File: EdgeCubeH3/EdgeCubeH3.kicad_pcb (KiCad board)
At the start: 2 copper layers, 52 x 52 mm, 19 parts, among them U1 H3, U2 K4B4G1646Q

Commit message: Schematic update, PCB started
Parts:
- added C11: 1u, Capacitor_SMD:C_0603_1608Metric, F.Cu at (184.1, 120.0)
- added C12: 10u, Capacitor_SMD:C_0603_1608Metric, F.Cu at (177.1, 122.0)
- added C13: 10u, Capacitor_SMD:C_0603_1608Metric, F.Cu at (174.1, 122.0)
- added C14: 22p, Capacitor_SMD:C_0603_1608Metric, F.Cu at (172.6, 115.7)
- added C15: 10u, Capacitor_SMD:C_0603_1608Metric, F.Cu at (177.0, 113.0)
- added C16: 10u, Capacitor_SMD:C_0603_1608Metric, F.Cu at (174.0, 113.0)
- added C17: 22p, Capacitor_SMD:C_0603_1608Metric, F.Cu at (172.5, 106.7)
- added C18: 10u, Capacitor_SMD:C_0603_1608Metric, F.Cu at (176.8, 104.0)
- added C19: 10u, Capacitor_SMD:C_0603_1608Metric, F.Cu at (173.8, 104.0)
- added C20: 15p, Capacitor_SMD:C_0603_1608Metric, F.Cu at (172.2, 97.6)
- added C21: 2u2, Capacitor_SMD:C_0603_1608Metric, F.Cu at (198.8, 120.0)
- added C22: 2u2, Capacitor_SMD:C_0603_1608Metric, F.Cu at (198.8, 122.5)
- added C23: 4u7, Capacitor_SMD:C_0603_1608Metric, F.Cu at (192.3, 84.5)
- added C24: 15p, Capacitor_SMD:C_0603_1608Metric, F.Cu at (160.3, 119.4)
- added C25: 15p, Capacitor_SMD:C_0603_1608Metric, F.Cu at (163.1, 117.0)
- added C26: 15p, Capacitor_SMD:C_0603_1608Metric, F.Cu at (164.8, 114.5)
- added C27: 15p, Capacitor_SMD:C_0603_1608Metric, F.Cu at (164.8, 109.5)
- added C28: 100n, Capacitor_SMD:C_0402_1005Metric, F.Cu at (199.7, 94.3)
- added C29: 4u7, Capacitor_SMD:C_0603_1608Metric, F.Cu at (192.3, 97.0)
- added C30: 100n, Capacitor_SMD:C_0603_1608Metric, F.Cu at (196.3, 84.5)
- added C31: 100n, Capacitor_SMD:C_0402_1005Metric, F.Cu at (199.7, 96.3)
- added C32: 100n, Capacitor_SMD:C_0402_1005Metric, F.Cu at (199.7, 98.3)
- added C33: 100n, Capacitor_SMD:C_0402_1005Metric, F.Cu at (199.7, 100.2)
- added C34: 100n, Capacitor_SMD:C_0402_1005Metric, F.Cu at (199.7, 102.2)
- added C35: 10u, Capacitor_SMD:C_0603_1608Metric, F.Cu at (196.3, 87.0)
- added C36: 10u, Capacitor_SMD:C_0603_1608Metric, F.Cu at (196.3, 89.5)
- added C37: 100n, Capacitor_SMD:C_0402_1005Metric, F.Cu at (202.6, 94.3)
- added C38: 10u, Capacitor_SMD:C_0603_1608Metric, F.Cu at (196.3, 92.0)
- added C39: 100n, Capacitor_SMD:C_0402_1005Metric, F.Cu at (202.6, 96.3)
- added C40: 100n, Capacitor_SMD:C_0402_1005Metric, F.Cu at (202.6, 98.3)
- added C41: 100n, Capacitor_SMD:C_0402_1005Metric, F.Cu at (202.6, 100.2)
- added C42: 100n, Capacitor_SMD:C_0402_1005Metric, F.Cu at (202.6, 102.2)
- added C43: 1u, Capacitor_SMD:C_0603_1608Metric, F.Cu at (139.0, 112.8)
- added C44: 1u, Capacitor_SMD:C_0603_1608Metric, B.Cu at (139.9, 89.0)
- added D1: SS12, Diode_SMD:D_SMA, F.Cu at (175.0, 90.6)
- added D2: 1N5819WS, Diode_SMD:D_SOD-323, B.Cu at (147.9, 125.8)
- added D4: LED, LED_SMD:LED_0805_2012Metric, F.Cu at (207.0, 129.0)
- added D5: LED, LED_SMD:LED_0805_2012Metric, F.Cu at (207.0, 132.0)
- added J1: USB PWR, Connector_USB:USB_C_Receptacle_HRO_TYPE-C-31-M-12, F.Cu at (137.9, 80.6)
- added J3: USB_A_Stacked, Connector_USB:USB_A_CUI_UJ2-ADH-TH_Horizontal_Stacked, F.Cu at (134.1, 95.5)
- added J4: GPDI_A, Connector_Video:HDMI_A_Molex_208658-1001_Horizontal, F.Cu at (152.9, 125.0)
- added J5: 93626-3006, rj45:936263006, F.Cu at (141.4, 114.5)
- added J6: DBG UART, Connector_PinHeader_2.54mm:PinHeader_1x03_P2.54mm_Vertical, B.Cu at (165.0, 122.8)
- added J7: GPIO, Connector_PinHeader_2.54mm:PinHeader_2x13_P2.54mm_Vertical, F.Cu at (177.2, 79.9)
- added J8: Micro_SD_Card_Det1, icepi:microSD_TF-01A, B.Cu at (172.2, 93.1)
- added L1: 2u2, Inductor_SMD:L_APV_APH0420, F.Cu at (170.2, 119.6)
- added L2: 2u2, Inductor_SMD:L_APV_APH0420, F.Cu at (170.1, 110.6)
- added L3: 2u2, Inductor_SMD:L_APV_APH0420, F.Cu at (169.8, 101.6)
- added Q1: NPN, Package_TO_SOT_SMD:TSOT-23, F.Cu at (176.0, 94.2)
- added Q2: PMOS, Package_TO_SOT_SMD:SOT-23W, F.Cu at (189.0, 126.0)
- added Q3: AO3404, Package_TO_SOT_SMD:SOT-23, B.Cu at (152.2, 125.9)
- added Q4: NPN, Package_TO_SOT_SMD:TSOT-23, F.Cu at (206.7, 104.9)
- added R10: 200K, Capacitor_SMD:C_0603_1608Metric, F.Cu at (175.7, 106.7)
- added R11: 100K, Capacitor_SMD:C_0603_1608Metric, F.Cu at (177.3, 106.7)
- added R12: 300K, Capacitor_SMD:C_0603_1608Metric, F.Cu at (174.1, 106.7)
- added R13: 10K, Resistor_SMD:R_0603_1608Metric, F.Cu at (173.8, 97.6)
- added R14: 12K, Resistor_SMD:R_0603_1608Metric, F.Cu at (175.4, 97.6)
- added R15: 33K, Resistor_SMD:R_0603_1608Metric, F.Cu at (177.0, 97.8)
- added R16: 33K, Resistor_SMD:R_0603_1608Metric, F.Cu at (173.0, 94.2)
- added R17: 10K, Resistor_SMD:R_0603_1608Metric, F.Cu at (169.2, 106.6)
- added R18: 10K, Resistor_SMD:R_0603_1608Metric, F.Cu at (171.5, 94.2)
- added R19: 100K, Resistor_SMD:R_0805_2012Metric_Pad1.20x1.40mm_HandSolder, F.Cu at (187.0, 131.0)
- added R20: 5K6, Resistor_SMD:R_0603_1608Metric, F.Cu at (198.8, 125.0)
- added R21: 2K, Resistor_SMD:R_0603_1608Metric, F.Cu at (198.8, 127.5)
- added R22: 2K, Resistor_SMD:R_0603_1608Metric, F.Cu at (198.8, 130.0)
- added R23: 30K, Resistor_SMD:R_0603_1608Metric, B.Cu at (155.9, 125.8)
- added R24: 5K6, Resistor_SMD:R_0603_1608Metric_Pad0.98x0.95mm_HandSolder, F.Cu at (188.1, 84.5)
- added R25: 470R, Resistor_SMD:R_0603_1608Metric_Pad0.98x0.95mm_HandSolder, F.Cu at (188.1, 87.0)
- added R26: 470R, Resistor_SMD:R_0603_1608Metric, B.Cu at (129.8, 122.0)
- added R27: 470R, Resistor_SMD:R_0603_1608Metric, B.Cu at (129.8, 118.4)
- added R28: 470R, Resistor_SMD:R_0603_1608Metric, F.Cu at (202.8, 125.0)
- added R29: 470R, Resistor_SMD:R_0603_1608Metric, F.Cu at (202.8, 127.5)
- added R30: 120R, Resistor_SMD:R_0603_1608Metric, F.Cu at (168.0, 127.9)
- added R31: 120R, Resistor_SMD:R_0603_1608Metric, F.Cu at (168.0, 125.4)
- added R32: 10K, Resistor_SMD:R_0603_1608Metric, F.Cu at (206.8, 120.0)
- added R33: 33R, Resistor_SMD:R_0603_1608Metric_Pad0.98x0.95mm_HandSolder, F.Cu at (188.1, 89.5)
- added R34: 47K, Resistor_SMD:R_0603_1608Metric, F.Cu at (206.8, 122.5)
- added R35: 47K, Resistor_SMD:R_0603_1608Metric, F.Cu at (206.8, 125.0)
- added R36: 56K, Resistor_SMD:R_0603_1608Metric_Pad0.98x0.95mm_HandSolder, F.Cu at (188.1, 92.0)
- added R37: 10K, Resistor_SMD:R_0603_1608Metric_Pad0.98x0.95mm_HandSolder, F.Cu at (188.1, 94.5)
- added R38: 10K, Resistor_SMD:R_0603_1608Metric_Pad0.98x0.95mm_HandSolder, F.Cu at (188.1, 97.0)
- added R39: 10K, Resistor_SMD:R_0603_1608Metric_Pad0.98x0.95mm_HandSolder, F.Cu at (188.1, 99.5)
- added R40: 51K, Resistor_SMD:R_0603_1608Metric_Pad0.98x0.95mm_HandSolder, F.Cu at (188.1, 102.1)
- added R41: 51K, Resistor_SMD:R_0603_1608Metric_Pad0.98x0.95mm_HandSolder, F.Cu at (188.1, 104.6)
- added R42: 10M, Resistor_SMD:R_0603_1608Metric, F.Cu at (167.8, 107.5)
- added R43: 3K, Resistor_SMD:R_0603_1608Metric, F.Cu at (158.2, 68.6)
- added R44: 3K, Resistor_SMD:R_0603_1608Metric, F.Cu at (158.2, 71.1)
- added R45: 3K, Resistor_SMD:R_0603_1608Metric, F.Cu at (158.2, 73.6)
- added R46: 3K, Resistor_SMD:R_0603_1608Metric, F.Cu at (158.2, 76.1)
- added R6: 10R, Resistor_SMD:R_1206_3216Metric, F.Cu at (173.9, 87.6)
- added R7: 680K, Capacitor_SMD:C_0603_1608Metric, F.Cu at (175.8, 115.7)
- added R8: 75K, Capacitor_SMD:C_0603_1608Metric, F.Cu at (177.4, 115.7)
- added R9: 680K, Capacitor_SMD:C_0603_1608Metric, F.Cu at (174.2, 115.7)
- added SW1: RST, Button_Switch_SMD:Button_6x3mm, F.Cu at (203.3, 85.8)
- added SW2: PWR, Button_Switch_SMD:Button_6x3mm, F.Cu at (203.3, 90.8)
- added TP1: UBOOT, TestPoint:TestPoint_Pad_D1.0mm, F.Cu at (205.5, 94.9)
- added TP2: PWR_KEY, TestPoint:TestPoint_Pad_D1.0mm, F.Cu at (205.5, 97.9)
- added TP3: TV, TestPoint:TestPoint_Pad_D1.0mm, F.Cu at (205.5, 101.0)
- added TP4: supercap, TestPoint:TestPoint_Pad_1.0x1.0mm, F.Cu at (174.9, 85.3)
- added TP5: gnd, TestPoint:TestPoint_Pad_1.0x1.0mm, F.Cu at (177.3, 85.2)
- added U10: USBLC6-4SC6, Package_TO_SOT_SMD:SOT-23-6, B.Cu at (141.4, 99.4)
- added U11: USBLC6-4SC6, Package_TO_SOT_SMD:SOT-23-6, F.Cu at (155.4, 117.4)
- added U12: USBLC6-4SC6, Package_TO_SOT_SMD:SOT-23-6, F.Cu at (151.6, 117.4)
- added U13: USBLC6-4SC6, Package_TO_SOT_SMD:SOT-23-6, F.Cu at (147.8, 117.4)
- added U3: USBLC6-2SC6, Package_TO_SOT_SMD:SOT-23-6, B.Cu at (137.7, 80.7)
- added U4: SY6280AAC, Package_TO_SOT_SMD:SOT-23-5, B.Cu at (130.0, 99.0)
- added U5: SY8089AAAC, SY8089:SY8089AAAC_SGY, F.Cu at (176.4, 119.3)
- added U6: SY8089AAAC, SY8089:SY8089AAAC_SGY, F.Cu at (176.3, 110.3)
- added U7: SY8032, Package_TO_SOT_SMD:SOT-23-6, F.Cu at (176.0, 101.4)
- added U8: W25Q128JVP, Package_SON:WSON-8-1EP_6x5mm_P1.27mm_EP3.4x4.3mm, B.Cu at (144.2, 90.4)
- added Y1: 24M, Crystal:Crystal_SMD_3225-4Pin_3.2x2.5mm, F.Cu at (160.2, 116.9)
- added Y2: 32K, Crystal:Crystal_SMD_3225-4Pin_3.2x2.5mm, F.Cu at (164.8, 112.0)
- U1: footprint Lib:BGA347_H3_AWT-M -> cm0:FBGA-347_14x14mm_Layout21x21_P0.65mm
- moved C2 34.0 mm to (185.6, 113.8)
- moved C9 34.0 mm to (193.1, 113.8)
- moved C1 34.0 mm to (183.1, 113.8)
- moved C10 34.0 mm to (195.6, 113.8)
- moved C3 34.0 mm to (182.8, 110.4)
- moved C4 34.0 mm to (184.8, 110.4)
- moved C5 34.0 mm to (186.7, 110.4)
- moved C6 34.0 mm to (188.7, 110.4)
- moved C7 34.0 mm to (188.1, 113.8)
- moved C8 34.0 mm to (190.6, 113.8)
- moved R3 34.0 mm to (198.1, 113.8)
- moved R4 34.0 mm to (200.6, 113.8)
- moved R5 34.0 mm to (203.2, 113.8)
- moved U1 14.4 mm to (154.2, 106.5), turned to 90 degrees
- moved U2 7.26 mm to (157.0, 91.0), turned to 90 degrees
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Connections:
- net VDD_DRAM renamed +1V35
- U1 pad A19: unconnected-(U1F-PF1-PadA19) -> /SoC/SDC0_D0
- U1 pad A2: unconnected-(U1D-EPHY_LINK_LED-PadA2) -> /SoC/EPHY_LINK_LED
- U1 pad A21: Net-(U1B-GND-PadA21) -> GND
- U1 pad A3: unconnected-(U1D-EPHY_TXN-PadA3) -> /SoC/EPHY_TX-
- U1 pad A4: unconnected-(U1D-EPHY_RXN-PadA4) -> /SoC/EPHY_RX-
- U1 pad A5: unconnected-(U1E-USB_D0+-PadA5) -> USB_D0+
- U1 pad A7: unconnected-(U1E-USB_D2+-PadA7) -> USB_D2+
- U1 pad A8: unconnected-(U1E-USB_D2--PadA8) -> USB_D2-
- U1 pad AA1: Net-(U1B-GND-PadA21) -> GND
- U1 pad AA6: unconnected-(U1G-NMI-PadAA6) -> Net-(U1G-NMI)
- U1 pad B13: unconnected-(U1F-PA18-PadB13) -> TWI1_SCK
- U1 pad B14: unconnected-(U1F-PA19-PadB14) -> TWI1_SDA
- U1 pad B15: unconnected-(U1C-PC3-PadB15) -> SPI0_CS
- U1 pad B16: unconnected-(U1C-PC2-PadB16) -> SPI0_CLK
- U1 pad B3: unconnected-(U1D-EPHY_TXP-PadB3) -> /SoC/EPHY_TX+
- U1 pad B4: unconnected-(U1D-EPHY_RXP-PadB4) -> /SoC/EPHY_RX+
- U1 pad B5: unconnected-(U1E-USB_D0--PadB5) -> USB_D0-
- U1 pad B6: unconnected-(U1E-USB_D1+-PadB6) -> USB_D1+
- U1 pad B7: unconnected-(U1E-USB_D1--PadB7) -> USB_D1-
- U1 pad C13: unconnected-(U1F-PA12-PadC13) -> TWI0_SDA
- U1 pad C14: unconnected-(U1F-PA17-PadC14) -> STATUS_LED
- U1 pad C15: unconnected-(U1C-PC0-PadC15) -> SPI0_MOSI
- U1 pad C16: unconnected-(U1C-PC1-PadC16) -> SPI0_MISO
- U1 pad C20: unconnected-(U1F-PF5-PadC20) -> /SoC/SDC0_D2
- U1 pad D11: unconnected-(U1F-PA0-PadD11) -> UART2_TX
- U1 pad D15: unconnected-(U1F-PA16-PadD15) -> SPI1_MISO
- U1 pad D19: unconnected-(U1F-PF0-PadD19) -> /SoC/SDC0_D1
- U1 pad D20: unconnected-(U1F-PF2-PadD20) -> Net-(U1F-PF2)
- U1 pad D3: unconnected-(U1C-PG7-PadD3) -> UART1_RX
- U1 pad D5: unconnected-(U1F-PA1-PadD5) -> UART2_RX
- U1 pad D6: unconnected-(U1F-PA2-PadD6) -> UART2_RTS
- U1 pad D8: unconnected-(U1F-PA7-PadD8) -> PA7
- U1 pad E11: unconnected-(U1F-PA10-PadE11) -> PA10
- U1 pad E13: unconnected-(U1F-PA3-PadE13) -> UART2_CTS
- U1 pad E14: unconnected-(U1F-PA6-PadE14) -> PA6
- U1 pad E15: unconnected-(U1F-PA13-PadE15) -> SPI1_CS
- U1 pad E2: unconnected-(U1D-GPDI_CLK--PadE2) -> /SoC/GPDI_CLK-
- U1 pad E21: unconnected-(U1F-PF4-PadE21) -> /SoC/SDC0_D3
- U1 pad F1: unconnected-(U1D-GPDI_D0--PadF1) -> /SoC/GPDI_D0-
- U1 pad F10: unconnected-(U1D-TVOUT-PadF10) -> Net-(U1D-TVOUT)
- U1 pad F11: unconnected-(U1F-PA11-PadF11) -> TWI0_SCK
- U1 pad F14: unconnected-(U1F-PA15-PadF14) -> SPI1_MOSI
- U1 pad F18: unconnected-(U1F-PF3-PadF18) -> /SoC/SDC0_CMD
- U1 pad F2: unconnected-(U1D-GPDI_CLK+-PadF2) -> /SoC/GPDI_CLK+
- U1 pad F5: unconnected-(U1F-PA4-PadF5) -> UART0_TX
- U1 pad F6: unconnected-(U1D-EPHY_RTX-PadF6) -> Net-(U1D-EPHY_RTX)
- U1 pad F7: unconnected-(U1D-EPHY_SPD_LED-PadF7) -> /SoC/EPHY_SPD_LED
- U1 pad F8: unconnected-(U1D-EPHY_VDD-PadF8) -> +1V2
- U1 pad G1: unconnected-(U1D-GPDI_D0+-PadG1) -> /SoC/GPDI_D0+
- U1 pad G10: unconnected-(U1B-VDD-EFUSE-PadG10) -> Net-(U1B-VDD-EFUSE)
- U1 pad G11: unconnected-(U1E-VCC_USB-PadG11) -> VCC_IO
- U1 pad G12: unconnected-(U1F-PA14-PadG12) -> SPI1_CLK
- U1 pad G13: unconnected-(U1B-VCC-IO-PadG13) -> VCC_IO
- U1 pad G14: unconnected-(U1B-VCC-IO-PadG14) -> VCC_IO
- U1 pad G15: unconnected-(U1B-VCC-IO-PadG15) -> VCC_IO
- U1 pad G18: unconnected-(U1F-PF6-PadG18) -> /SoC/SDC0_DET
- U1 pad G2: unconnected-(U1D-GPDI_D1--PadG2) -> /SoC/GPDI_D1-
- U1 pad G4: unconnected-(U1C-PG6-PadG4) -> UART1_TX
- U1 pad G5: unconnected-(U1D-GPDI_CEC-PadG5) -> /SoC/GPDI_CEC
- U1 pad G7: unconnected-(U1D-EPHY_VCC-PadG7) -> +3V3
- U1 pad G8: Net-(U1B-GND-PadA21) -> GND
- U1 pad G9: unconnected-(U1D-V33_TV-PadG9) -> +3V3
- U1 pad H10: unconnected-(U1B-VDD-SYS-PadH10) -> +1V2
- U1 pad H11: unconnected-(U1B-VDD-EFUSEEBP-PadH11) -> +3V3
- U1 pad H12: Net-(U1B-GND-PadA21) -> GND
- U1 pad H13: unconnected-(U1B-VCC-IO-PadH13) -> VCC_IO
- U1 pad H14: unconnected-(U1B-VCC-IO-PadH14) -> VCC_IO
- U1 pad H15: Net-(U1B-GND-PadA21) -> GND
- U1 pad H2: unconnected-(U1D-GPDI_D1+-PadH2) -> /SoC/GPDI_D1+
- U1 pad H3: unconnected-(U1D-GPDI_SCL-PadH3) -> /SoC/GPDI_SCL
- U1 pad H6: unconnected-(U1F-PA5-PadH6) -> UART0_RX
- U1 pad H7: unconnected-(U1C-VCC-PG-PadH7) -> VCC_IO
- U1 pad H8: unconnected-(U1D-GND_TV-PadH8) -> GND
- U1 pad J1: unconnected-(U1D-GPDI_D2+-PadJ1) -> /SoC/GPDI_D2+
- U1 pad J10: unconnected-(U1B-VDD-SYS-PadJ10) -> +1V2
- U1 pad J11: unconnected-(U1B-VDD-SYS-PadJ11) -> +1V2
- U1 pad J12: unconnected-(U1B-VDD-SYS-PadJ12) -> +1V2
- U1 pad J13: Net-(U1B-GND-PadA21) -> GND
- U1 pad J14: unconnected-(U1B-VCC-IO-PadJ14) -> VCC_IO
- U1 pad J15: unconnected-(U1F-VCC_PD-PadJ15) -> VCC_IO
- U1 pad J16: Net-(U1B-GND-PadA21) -> GND
- U1 pad J2: unconnected-(U1D-GPDI_D2--PadJ2) -> /SoC/GPDI_D2-
- U1 pad J6: unconnected-(U1D-GPDI_VCC-PadJ6) -> +3V3
- U1 pad J7: unconnected-(U1B-VDD-CPUS-PadJ7) -> +1V2
- U1 pad J8: unconnected-(U1B-VDD-CPUS-PadJ8) -> +1V2
- U1 pad J9: Net-(U1B-GND-PadA21) -> GND
- U1 pad K1: unconnected-(U1G-X24MOUT-PadK1) -> Net-(U1G-X24MOUT)
- U1 pad K10: unconnected-(U1B-VDD-SYS-PadK10) -> +1V2
- U1 pad K11: unconnected-(U1B-VDD-SYS-PadK11) -> +1V2
- U1 pad K12: unconnected-(U1B-VDD-SYS-PadK12) -> +1V2
- U1 pad K13: Net-(U1B-GND-PadA21) -> GND
- U1 pad K14: Net-(U1B-GND-PadA21) -> GND
- U1 pad K15: Net-(U1B-GND-PadA21) -> GND
- U1 pad K16: Net-(U1B-GND-PadA21) -> GND
- U1 pad K2: unconnected-(U1G-X24MIN-PadK2) -> Net-(U1G-X24MIN)
- U1 pad K3: unconnected-(U1D-GPDI_SDA-PadK3) -> /SoC/GPDI_SDA
- U1 pad K6: unconnected-(U1G-VCC_RTC-PadK6) -> +3V3
- U1 pad K7: Net-(U1B-GND-PadA21) -> GND
- U1 pad K8: Net-(U1B-GND-PadA21) -> GND
- U1 pad K9: Net-(U1B-GND-PadA21) -> GND
- U1 pad L10: unconnected-(U1B-VDD-SYS-PadL10) -> +1V2
- U1 pad L11: unconnected-(U1B-VDD-SYS-PadL11) -> +1V2
- U1 pad L12: unconnected-(U1B-VDD-SYS-PadL12) -> +1V2
- U1 pad L13: unconnected-(U1B-VDD-SYS-PadL13) -> +1V2
- U1 pad L14: unconnected-(U1B-VDD-SYS-PadL14) -> +1V2
- U1 pad L15: Net-(U1B-GND-PadA21) -> GND
- U1 pad L8: Net-(U1B-GND-PadA21) -> GND
- U1 pad L9: Net-(U1B-GND-PadA21) -> GND
- U1 pad M10: Net-(U1B-GND-PadA21) -> GND
- U1 pad M11: Net-(U1B-GND-PadA21) -> GND
- U1 pad M12: Net-(U1B-GND-PadA21) -> GND
- U1 pad M13: Net-(U1B-GND-PadA21) -> GND
- U1 pad M14: Net-(U1B-GND-PadA21) -> GND
- U1 pad M15: Net-(U1B-GND-PadA21) -> GND
- U1 pad M2: unconnected-(U1D-GPDI_HPD-PadM2) -> /SoC/GPDI_HPD
- U1 pad M4: unconnected-(U1G-RTC_VIO-PadM4) -> +1V2
- U1 pad M5: unconnected-(U1D-GPDI_GND-PadM5) -> GND
- U1 pad M6: unconnected-(U1F-PL9-PadM6) -> PWR_DRAM_EN
- U1 pad M7: Net-(U1B-GND-PadA21) -> GND
- U1 pad M8: Net-(U1B-GND-PadA21) -> GND
- U1 pad M9: Net-(U1B-GND-PadA21) -> GND
- U1 pad N10: Net-(U1B-GND-PadA21) -> GND
- U1 pad N11: Net-(U1B-GND-PadA21) -> GND
- U1 pad N12: Net-(U1B-GND-PadA21) -> GND
- U1 pad N13: Net-(U1B-GND-PadA21) -> GND
- U1 pad N14: Net-(U1B-GND-PadA21) -> GND
- U1 pad N15: Net-(U1B-GND-PadA21) -> GND
- U1 pad N2: unconnected-(U1F-PL4-PadN2) -> Net-(U1F-PL4)
- U1 pad N3: unconnected-(U1G-VCC_PLL-PadN3) -> +3V3
- U1 pad N7: Net-(U1B-GND-PadA21) -> GND
- U1 pad N8: unconnected-(U1B-VDD-CPUX-PadN8) -> +1V2
- U1 pad N9: Net-(U1B-GND-PadA21) -> GND
- U1 pad P10: Net-(U1B-GND-PadA21) -> GND
- U1 pad P11: Net-(U1B-GND-PadA21) -> GND
- U1 pad P12: Net-(U1B-GND-PadA21) -> GND
- U1 pad P13: Net-(U1B-GND-PadA21) -> GND
- U1 pad P14: Net-(U1B-GND-PadA21) -> GND
- U1 pad P15: Net-(U1B-GND-PadA21) -> GND
- U1 pad P6: unconnected-(U1B-VDD-CPUX-PadP6) -> +1V2
- U1 pad P7: unconnected-(U1B-VDD-CPUX-PadP7) -> +1V2
- U1 pad P8: unconnected-(U1B-VDD-CPUX-PadP8) -> +1V2
- U1 pad P9: unconnected-(U1B-VDD-CPUX-PadP9) -> +1V2
- U1 pad R1: unconnected-(U1F-PL3-PadR1) -> Net-(U1F-PL3)
- U1 pad R10: Net-(U1B-GND-PadA21) -> GND
- U1 pad R11: Net-(U1B-GND-PadA21) -> GND
- U1 pad R12: Net-(U1B-GND-PadA21) -> GND
- U1 pad R13: Net-(U1B-GND-PadA21) -> GND
- U1 pad R14: Net-(U1B-GND-PadA21) -> GND
- U1 pad R2: unconnected-(U1F-PL5-PadR2) -> VCC_IO_EN
- U1 pad R6: unconnected-(U1B-VDD-CPUX-PadR6) -> +1V2
- U1 pad R7: unconnected-(U1B-VDD-CPUX-PadR7) -> +1V2
- U1 pad R8: unconnected-(U1B-VDD-CPUX-PadR8) -> +1V2
- U1 pad R9: Net-(U1B-GND-PadA21) -> GND
- U1 pad T10: unconnected-(U1G-VDD-CPUFB-PadT10) -> PWR_CPUFB
- U1 pad T11: Net-(U1B-GND-PadA21) -> GND
- U1 pad T2: unconnected-(U1F-PL8-PadT2) -> PWR_STB_EN
- U1 pad T4: unconnected-(U1F-PL6-PadT4) -> CPUX_VSET
- U1 pad T6: unconnected-(U1B-VDD-CPUX-PadT6) -> +1V2
- U1 pad T7: unconnected-(U1B-VDD-CPUX-PadT7) -> +1V2
- U1 pad T8: unconnected-(U1B-VDD-CPUX-PadT8) -> +1V2
- U1 pad T9: unconnected-(U1G-GND-CPUFB-PadT9) -> GND
- U1 pad U3: unconnected-(U1H-AGND-PadU3) -> GND
- U1 pad U4: unconnected-(U1G-X32KOUT-PadU4) -> Net-(U1G-X32KOUT)
- U1 pad U6: unconnected-(U1B-VDD-CPUX-PadU6) -> +1V2
- U1 pad U9: unconnected-(U1B-VDD-CPUX-PadU9) -> +1V2
- U1 pad V2: unconnected-(U1F-PL10-PadV2) -> PWR_LED
- U1 pad V3: unconnected-(U1H-AVCC-PadV3) -> +3V3
- U1 pad V5: unconnected-(U1G-X32KIN-PadV5) -> Net-(U1G-X32KIN)
- U1 pad V6: unconnected-(U1G-RESET-PadV6) -> /SoC/RESET
- U1 pad W6: unconnected-(U1G-UBOOT-PadW6) -> Net-(U1G-UBOOT)
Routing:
- net GND: track 0.00 -> 64.4 mm, vias 0 -> 53
- net /SoC/GPDI_CEC: track 0.00 -> 24.5 mm, vias 0 -> 1
- net /SoC/GPDI_SDA: track 0.00 -> 22.7 mm, vias 0 -> 2
- net PWR_DRAM_EN: track 0.00 -> 22.1 mm
- net VBUS: track 0.00 -> 21.8 mm, vias 0 -> 1
- net +3V3: track 0.00 -> 21.5 mm
- net +1V35: track 0.00 -> 20.1 mm
- net +1V2: track 0.00 -> 19.8 mm, vias 0 -> 6
- net /SoC/GPDI_HPD: track 0.00 -> 17.7 mm, vias 0 -> 2
- net /SoC/GPDI_SCL: track 0.00 -> 16.0 mm
- net /ports/CEC: track 0.00 -> 15.8 mm, vias 0 -> 1
- net /SoC/GPDI_D2-: track 0.00 -> 12.2 mm
- net /SoC/GPDI_D1+: track 0.00 -> 11.9 mm
- net /SoC/GPDI_CLK+: track 0.00 -> 11.9 mm
- net /SoC/GPDI_D0-: track 0.00 -> 11.5 mm
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- added copper zone on F.Cu, net GND
- added copper zone on In1.Cu, net GND
- added copper zone on In4.Cu, net GND
- added copper zone on F.Cu, net Net-(U5-LX)
- added copper zone on F.Cu, net Net-(U6-LX)
- added copper zone on F.Cu, net Net-(U7-LX)
- added copper zone on F.Cu, net VBUS
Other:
- copper layers 2 -> 6

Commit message: PCB design at ~90%
- re-arrangement of components
- connecting dram
- connecting ports
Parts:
- C29, C30, C43, Q4, R20, R21, R22, R33, R37, R38, R39, R40, R41, R42: moved to B.Cu
- D4: value LED -> PWR
- D5: value LED -> STA
- R19: footprint Resistor_SMD:R_0805_2012Metric_Pad1.20x1.40mm_HandSolder -> Resistor_SMD:R_0603_1608Metric_Pad0.98x0.95mm_HandSolder
- R36: footprint Resistor_SMD:R_0603_1608Metric_Pad0.98x0.95mm_HandSolder -> Resistor_SMD:R_0603_1608Metric
- R5: footprint Resistor_SMD:R_0603_1608Metric -> Resistor_SMD:R_0402_1005Metric; moved to B.Cu
- U10: moved to F.Cu
- moved D4 89.8 mm to (128.7, 85.0)
- moved D5 89.7 mm to (128.7, 88.3)
- moved R28 81.4 mm to (131.9, 85.1), turned to 180 degrees
- moved R29 81.1 mm to (131.9, 88.2), turned to 180 degrees
- moved R20 72.1 mm to (130.6, 101.7)
- moved C21 63.5 mm to (139.9, 96.3), turned to -90 degrees
- moved C11 59.3 mm to (135.0, 86.7), turned to 180 degrees
- moved C23 52.9 mm to (144.3, 106.9), turned to 180 degrees
- moved R25 51.9 mm to (140.8, 108.5)
- moved R24 50.1 mm to (144.1, 108.5)
- moved R5 50.1 mm to (160.1, 88.2), turned to 0 degrees
- moved R21 49.3 mm to (149.5, 127.1), turned to -90 degrees
- moved R22 47.9 mm to (151.0, 127.1), turned to 90 degrees
- moved C30 44.9 mm to (172.9, 122.8)
- moved Q4 42.8 mm to (169.0, 125.1), turned to 180 degrees
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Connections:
- net Net-(J1-D+-PadA6) renamed /power/USB+
- net Net-(J1-D--PadA7) renamed /power/USB-
- U2 pad A3: /SoC/SDQ15 -> /SoC/SDQ12
- U2 pad A7: /SoC/SDQ12 -> /SoC/SDQ8
- U2 pad B8: /SoC/SDQ14 -> /SoC/SDQ9
- U2 pad C2: /SoC/SDQ11 -> /SoC/SDQ15
- U2 pad C3: /SoC/SDQ9 -> /SoC/SDQ14
- U2 pad D7: /SoC/SDQ8 -> /SoC/SDQ11
- U2 pad E3: /SoC/SDQ0 -> /SoC/SDQ5
- U2 pad F2: /SoC/SDQ2 -> /SoC/SDQ6
- U2 pad F7: /SoC/SDQ1 -> /SoC/SDQ2
- U2 pad F8: /SoC/SDQ3 -> /SoC/SDQ0
- U2 pad G2: /SoC/SDQ6 -> /SoC/SDQ3
- U2 pad H3: /SoC/SDQ4 -> /SoC/SDQ7
- U2 pad H7: /SoC/SDQ7 -> /SoC/SDQ4
- U2 pad H8: /SoC/SDQ5 -> /SoC/SDQ1
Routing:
- net USB_D0-: track 0.00 -> 45.9 mm, vias 0 -> 1
- net USB_D0+: track 0.00 -> 43.8 mm, vias 0 -> 1
- net GND: track 64.4 -> 106.2 mm, vias 53 -> 98
- net VREF: track 0.00 -> 36.3 mm, vias 0 -> 4
- net USB_D1-: track 0.00 -> 29.7 mm, vias 0 -> 2
- net USB_D1+: track 0.00 -> 29.2 mm, vias 0 -> 2
- net /SoC/SWE: track 0.00 -> 27.3 mm
- net /SoC/SBA0: track 0.00 -> 26.9 mm
- net /SoC/SBA2: track 0.00 -> 26.9 mm
- net /SoC/SCK+: track 0.00 -> 26.9 mm, vias 0 -> 2
- net /SoC/SCK-: track 0.00 -> 26.9 mm, vias 0 -> 2
- net /SoC/SA5: track 0.00 -> 26.9 mm
- net /SoC/SA3: track 0.00 -> 26.8 mm
- net PWR_CPUFB: track 1.62 -> 28.3 mm
- net /SoC/SA15: track 0.00 -> 26.0 mm, vias 0 -> 2
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
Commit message: PCB at 95%
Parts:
- removed SW1: RST, Button_Switch_SMD:Button_6x3mm
- removed SW2: PWR, Button_Switch_SMD:Button_6x3mm
- C22, C28, C3, C31, C32, C33, C34, C35, C36, C37, C38, C39, C4, C40, C41, C42, C5, C6, C7, C9, R34, R35, TP1, TP2, TP3: moved to B.Cu
- moved TP3 65.2 mm to (140.6, 107.2), turned to 180 degrees
- moved TP2 55.2 mm to (153.1, 115.0), turned to 180 degrees
- moved C37 53.0 mm to (151.2, 107.2)
- moved C10 52.8 mm to (151.1, 85.4), turned to -90 degrees
- moved C39 52.3 mm to (151.8, 108.5)
- moved C40 51.6 mm to (152.2, 109.5)
- moved C8 50.1 mm to (149.4, 85.4), turned to -90 degrees
- moved C41 49.4 mm to (154.2, 110.3)
- moved TP1 48.3 mm to (159.3, 108.9), turned to 180 degrees
- moved C9 47.9 mm to (154.8, 85.1), turned to 180 degrees
- moved C31 47.7 mm to (153.6, 108.6)
- moved C28 47.1 mm to (155.7, 111.0), turned to 90 degrees
- moved C42 46.0 mm to (156.7, 104.7), turned to 180 degrees
- moved C33 45.8 mm to (154.4, 107.1)
- moved R34 45.7 mm to (163.8, 107.2), turned to 180 degrees
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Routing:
- net VBUS: track 40.2 -> 201.2 mm, vias 6 -> 13
- net +3V3: track 29.8 -> 139.2 mm, vias 8 -> 13
- net PWR_LED: track 0.00 -> 94.4 mm, vias 0 -> 3
- net VCC_IO: track 12.8 -> 88.0 mm, vias 6 -> 8
- net /SoC/SDC0_DET: track 0.00 -> 56.0 mm, vias 0 -> 2
- net /SoC/SDC0_CMD: track 0.00 -> 42.7 mm, vias 0 -> 2
- net /SoC/SDC0_D0: track 0.00 -> 41.8 mm, vias 0 -> 2
- net TWI1_SCK: track 0.00 -> 41.6 mm, vias 0 -> 1
- net /SoC/SDC0_CLK: track 0.00 -> 37.0 mm, vias 0 -> 2
- net /SoC/SDC0_D1: track 0.00 -> 35.2 mm, vias 0 -> 2
- net /SoC/SDC0_D3: track 0.00 -> 32.8 mm, vias 0 -> 2
- net UART2_RTS: track 0.00 -> 30.8 mm, vias 0 -> 1
- net /SoC/EPHY_SPD_LED: track 0.00 -> 30.6 mm, vias 0 -> 1
- net SPI1_CLK: track 0.00 -> 29.8 mm
- net SPI1_MOSI: track 0.00 -> 29.1 mm, vias 0 -> 1
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- added copper zone on In2.Cu, net +1V2
- added copper zone on In2.Cu, net +1V35

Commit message: PCB at 98%
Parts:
- removed R43, R44, R45, R46: 3K, Resistor_SMD:R_0603_1608Metric
- moved R32 8.88 mm to (162.5, 123.4), turned to -90 degrees
- moved D5 0.22 mm to (128.9, 88.3)
- moved D4 0.20 mm to (128.9, 85.0)
- moved TP5 0.10 mm to (177.3, 85.3)
- moved R38 0.10 mm to (172.9, 129.1)
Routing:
- net VCC_IO: track 88.0 -> 158.4 mm, vias 8 -> 9
- net UART0_TX: track 0.00 -> 46.2 mm, vias 0 -> 2
- net UART0_RX: track 0.00 -> 45.9 mm
- net GND: track 122.7 -> 155.9 mm, vias 110 -> 114
- net /SoC/RESET: track 0.00 -> 25.4 mm, vias 0 -> 3
- net CPUX_VSET: track 1.74 -> 26.0 mm, vias 0 -> 2
- net VCC_IO_EN: track 1.69 -> 25.2 mm
- net PWR_DRAM_EN: track 22.1 -> 42.8 mm
- net PWR_STB_EN: track 8.21 -> 28.4 mm, vias 0 -> 2
- net +3V3: track 139.2 -> 144.4 mm
- net Net-(J6-Pin_3): track 2.18 -> 6.86 mm, vias 0 -> 1
- net +1V35: track 42.1 -> 46.7 mm
- net Net-(Q4-B): track 0.00 -> 4.28 mm
- net Net-(C29-Pad2): track 0.00 -> 3.22 mm

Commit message: Compleating PCB design
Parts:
- added C45: 100n, Resistor_SMD:R_0402_1005Metric, B.Cu at (155.8, 103.5)
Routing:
- net /SoC/SDC0_D2: track 28.5 -> 42.9 mm
- net /SoC/SDC0_D3: track 33.0 -> 41.9 mm
- net /SoC/SDC0_D1: track 35.6 -> 41.9 mm
- net /SoC/SDC0_CLK: track 37.0 -> 42.1 mm
- net GND: track 155.9 -> 156.8 mm
- net VREF: track 36.3 -> 37.0 mm
- added copper zone on In2.Cu, net GND
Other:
- board text added: "EdgeCubeH3"
- board text added: "EdgeCubeH3 rev.A"
- board text added: "Flash"
- board text added: "github.com/sentoxo/EdgeCubeH3 J.K. 20.05.2026 rev.A"

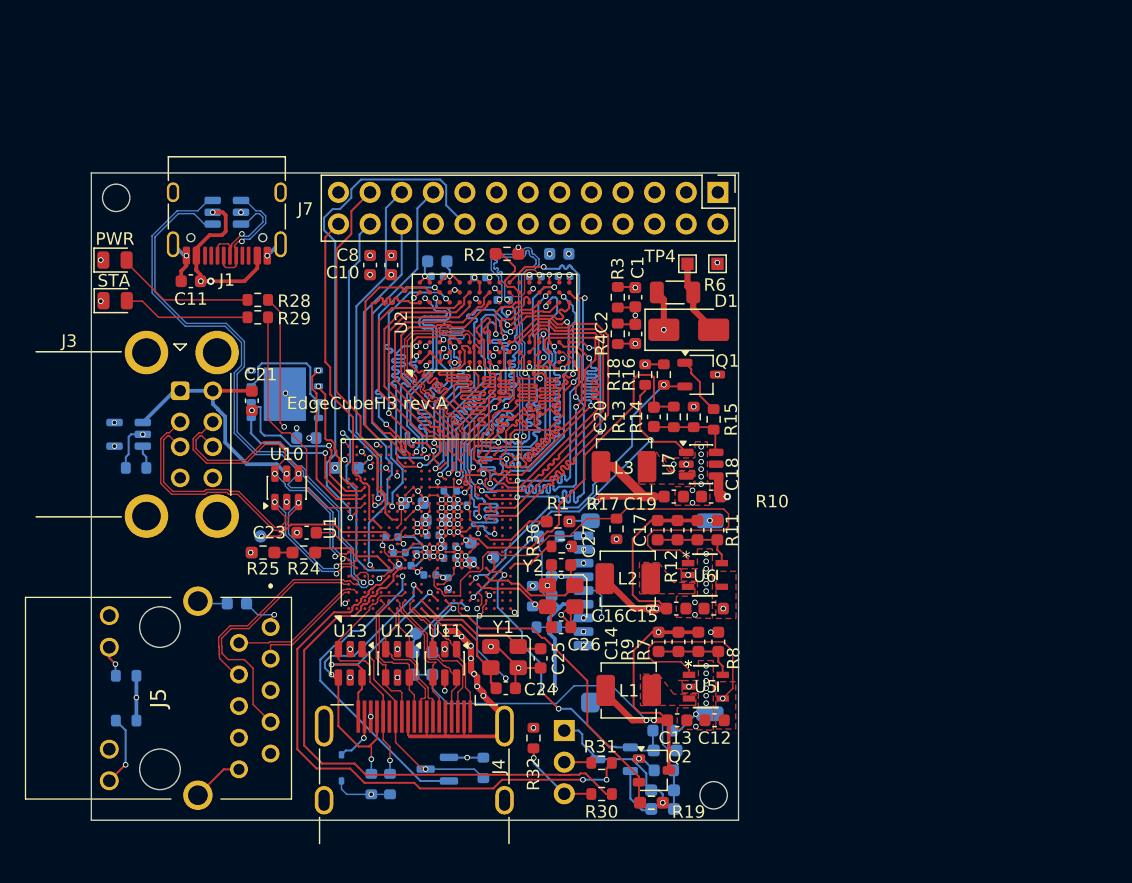
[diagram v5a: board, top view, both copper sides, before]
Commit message: Small changes to PCB, updated schematic and readme
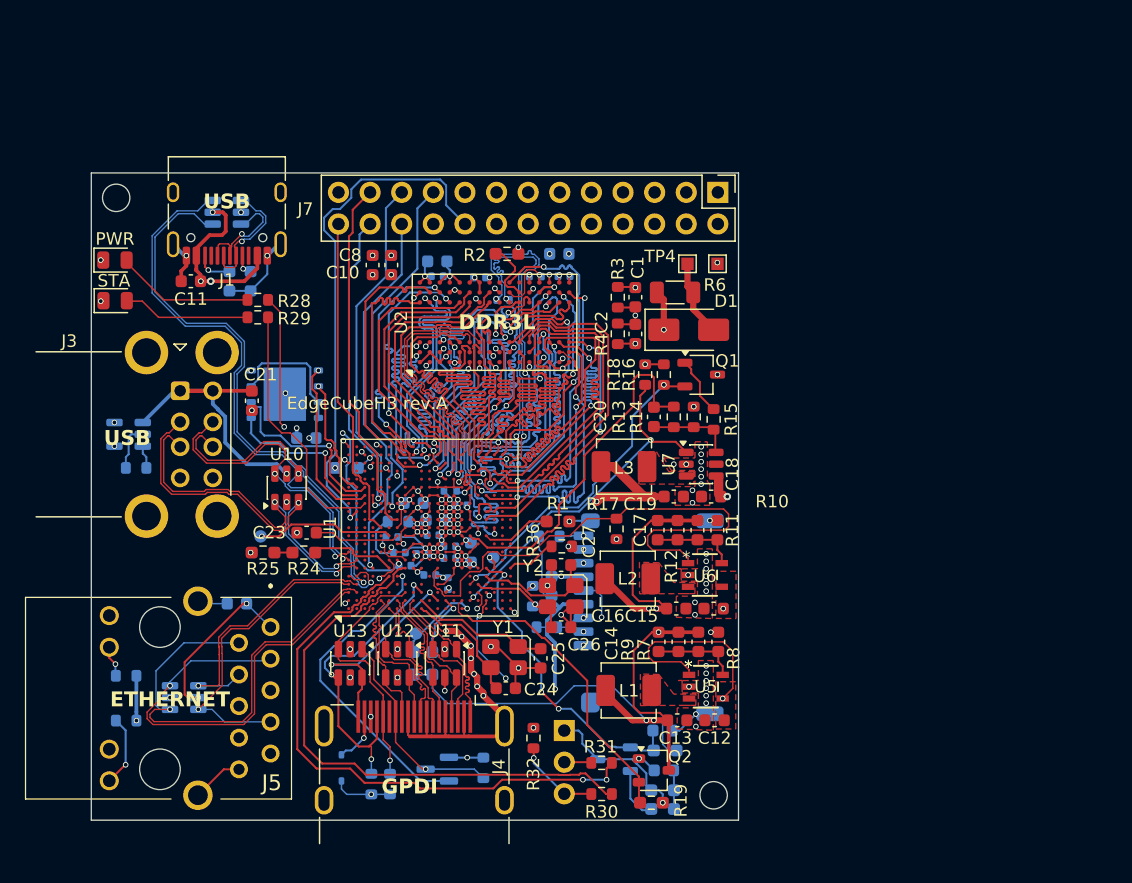
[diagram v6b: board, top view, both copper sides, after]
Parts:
- added R47: 2R2, Resistor_SMD:R_0603_1608Metric, B.Cu at (151.6, 106.0)
- added R48: 5K1, Capacitor_SMD:C_0603_1608Metric, B.Cu at (139.8, 86.7)
- added R49: 5K1, Capacitor_SMD:C_0603_1608Metric, B.Cu at (138.1, 86.7)
- added U14: USBLC6-4SC6, Package_TO_SOT_SMD:SOT-23-6, B.Cu at (134.5, 120.2)
- moved C8 0.20 mm to (149.6, 85.4)
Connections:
- C39 pad 1: +1V2 -> Net-(U1D-EPHY_VDD)
- J1 pad A5: unconnected-(J1-CC1-PadA5) -> Net-(J1-CC1)
- J1 pad B5: unconnected-(J1-CC2-PadB5) -> Net-(J1-CC2)
- U1 pad F8: +1V2 -> Net-(U1D-EPHY_VDD)
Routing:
- net +1V35: track 46.7 -> 88.8 mm
- net +1V2: track 39.5 -> 69.4 mm, vias 15 -> 14
- net /SoC/EPHY_TX-: track 9.13 -> 36.1 mm, vias 0 -> 1
- net /SoC/EPHY_TX+: track 11.4 -> 37.7 mm, vias 0 -> 1
- net VCC_IO: track 158.4 -> 169.3 mm, vias 9 -> 10
- net GND: track 156.8 -> 163.1 mm, vias 114 -> 115
- net /SoC/EPHY_RX+: track 17.1 -> 22.7 mm, vias 0 -> 1
- net Net-(J3-VBUS1): track 20.6 -> 25.8 mm
- net Net-(U1D-EPHY_VDD): track 0.00 -> 4.81 mm, vias 0 -> 1
- net /SoC/EPHY_RX-: track 21.2 -> 24.9 mm, vias 0 -> 1
- net Net-(J1-CC2): track 0.00 -> 3.01 mm, vias 0 -> 1
- net /SoC/GPDI_D0+: track 10.0 -> 12.0 mm
- net Net-(J1-CC1): track 0.00 -> 1.77 mm, vias 0 -> 1
- net /SoC/GPDI_D2+: track 10.8 -> 12.0 mm
- net SPI1_CLK: track 29.8 -> 29.0 mm
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- removed copper zone on In2.Cu, net +1V2
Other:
- board text added: "DDR3L"
- board text added: "ETHERNET"
- board text added: "G TX RX"
- board text added: "GPDI"
- board text added: "USB"
- board text added: "github.com/sentoxo/EdgeCubeH3 J.K. 21.05.2026 rev.A"
- board text added: "microSD"
- board text removed: "github.com/sentoxo/EdgeCubeH3 J.K. 20.05.2026 rev.A"

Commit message: Finalization of rev.A
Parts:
- removed TP4: supercap, TestPoint:TestPoint_Pad_1.0x1.0mm
- removed TP5: gnd, TestPoint:TestPoint_Pad_1.0x1.0mm
- added J2: SUPERCAP, Connector_PinHeader_1.27mm:PinHeader_1x02_P1.27mm_Vertical, F.Cu at (177.4, 85.5)
- J6: moved to F.Cu
- R48, R49: footprint Capacitor_SMD:C_0603_1608Metric -> Resistor_SMD:R_0603_1608Metric
- moved R32 14.6 mm to (177.1, 124.6), turned to 0 degrees
- turned J6 to 0 degrees
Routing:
- net Net-(J6-Pin_3): track 6.86 -> 15.7 mm, vias 1 -> 0
- net VCC_IO: track 169.3 -> 176.1 mm, vias 10 -> 9
- net SPI0_CLK: track 9.93 -> 16.0 mm
- net /SoC/SA0: track 24.9 -> 23.0 mm
- net GND: track 163.1 -> 164.9 mm, vias 115 -> 114
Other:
- board text added: "G"
- board text added: "RX"
- board text added: "TX"
- board text added: "USB-C"
- board text added: "github.com/sentoxo/EdgeCubeH3 J.K. 05/26 rev.A"
- board text added: "rev.A 05/26"
- board text removed: "EdgeCubeH3 rev.A"
- board text removed: "G TX RX"
- board text removed: "github.com/sentoxo/EdgeCubeH3 J.K. 21.05.2026 rev.A"
